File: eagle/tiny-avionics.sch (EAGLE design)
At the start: 67 parts, among them J1 USB-MICROB, J3 JST-PH-2-SMT-RA, U1 LP5907, U2 M25P10-AVMN6TP_TR, U3 LSM9DS0, U5 LTC1998, U6 ATMEGA32U4-AU, X1 8MHz

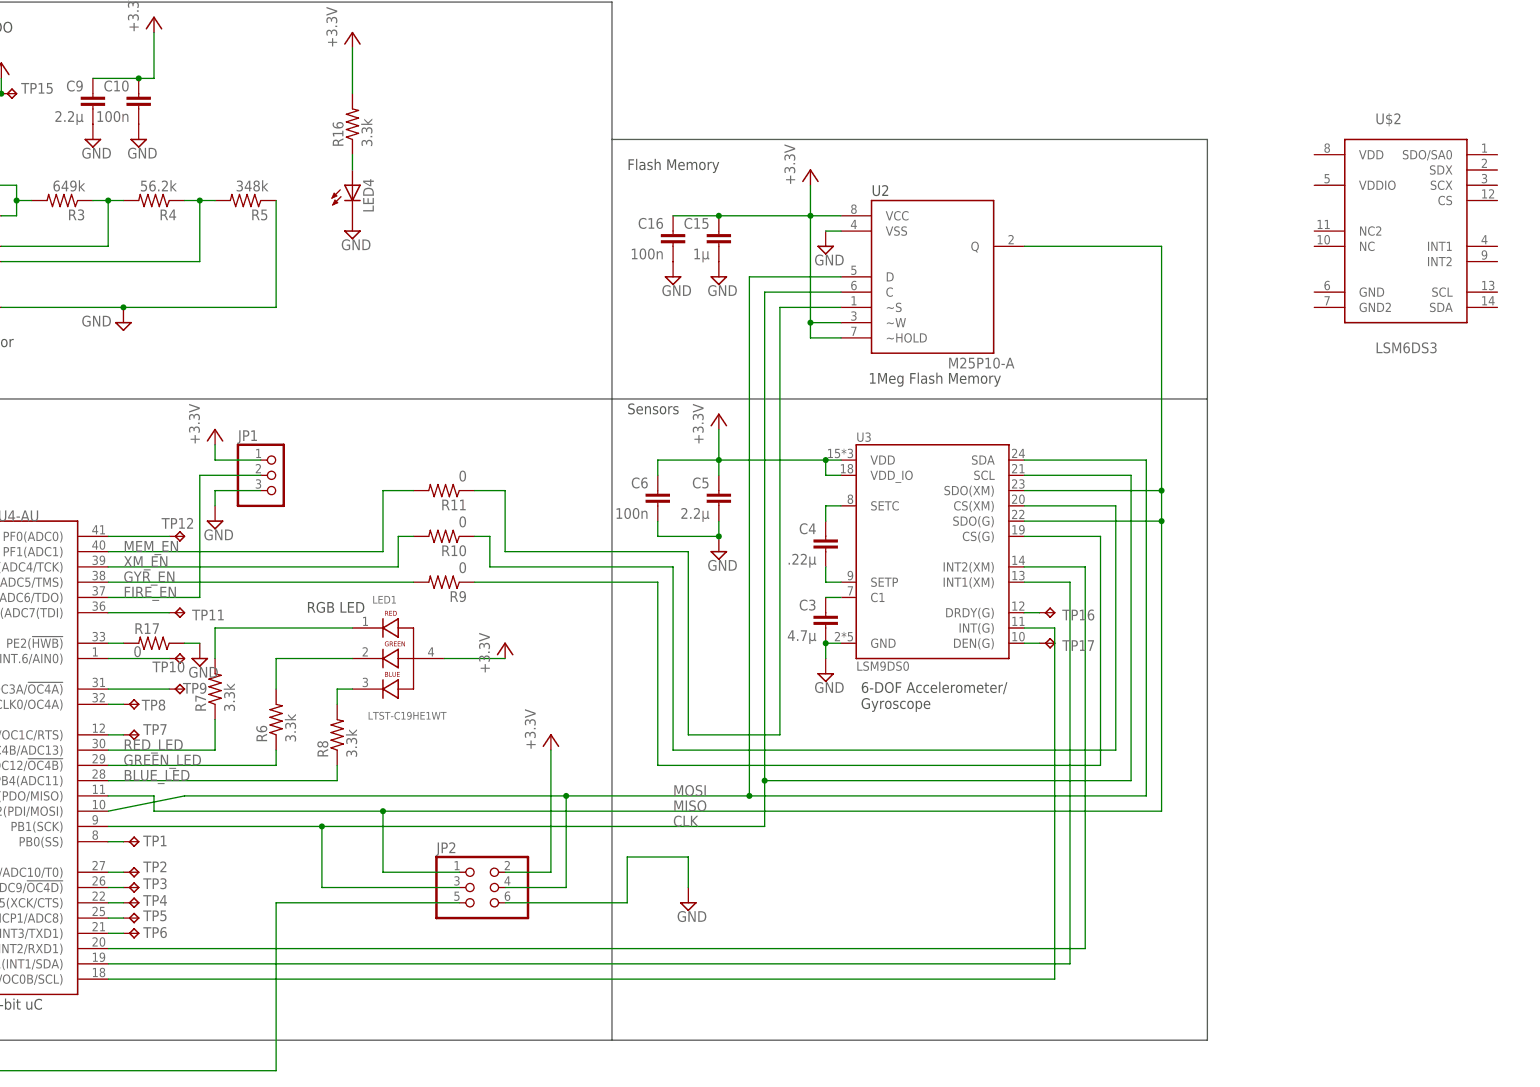
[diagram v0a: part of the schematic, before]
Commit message: Schematic work and created new device for 8-pin SPI memory chip.
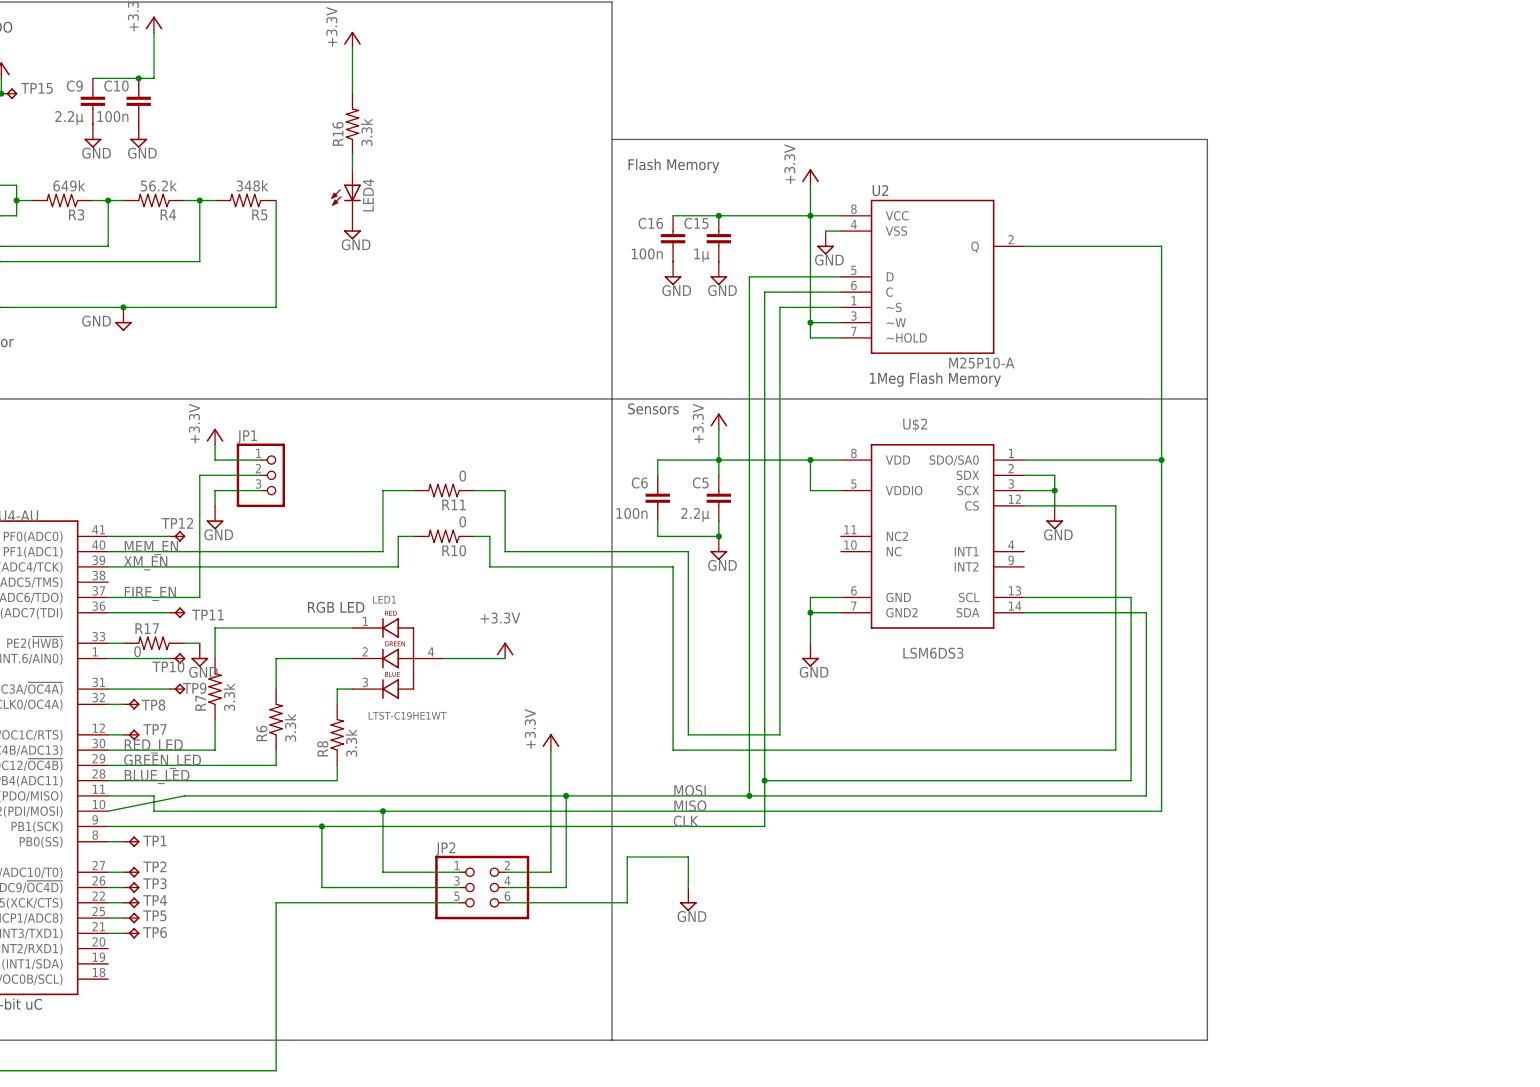
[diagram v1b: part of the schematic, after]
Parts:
- removed C3: 4.7µ, rcl:C-EUC0603
- removed C4: .22µ, rcl:C-EUC0603
- removed R9: 0, rcl:R-US_R0603
- removed TP16, TP17: TPTP08R, testpad:TPTP08R
- removed U3: LSM9DS0, LSM9DS0:LSM9DS0
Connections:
- removed net GYR_EN: R9.1, U3.CS(G)
- removed net N$10: C4.2, U3.SETC
- removed net N$11: C4.1, U3.SETP
- removed net N$16: U3.INT2(XM), U6.PD2(INT2/RXD1)
- removed net N$17: U3.INT1(XM), U6.PD1(INT1/SDA)
- removed net N$19: U3.INT(G), U6.PD0(INT0/OC0B/SCL)
- removed net N$20: R9.2, U6.PF5(ADC5/TMS)
- removed net N$66: TP17.TP, U3.DEN(G)
- removed net N$67: TP16.TP, U3.DRDY(G)
- removed net N$9: C3.2, U3.C1
- net CLK: now also U$2.SCL; no longer U3.SCL
- net GND: now also U$2.GND, U$2.GND2, U$2.SCX, U$2.SDX; no longer C3.1, U3.GND
- net MISO: now also U$2.SDO/SA0; no longer U3.SDO(G), U3.SDO(XM)
- net MOSI: now also U$2.SDA; no longer U3.SDA
- net VCC: now also U$2.VDD, U$2.VDDIO; no longer U3.VDD, U3.VDD_IO
- net XM_EN: now also U$2.CS; no longer U3.CS(XM)
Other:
- note removed: "6-DOF Accelerometer/ Gyroscope"
- moved on the sheet: U$2

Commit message: Working changes to schematic and layout.
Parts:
- removed U2: M25P10-AVMN6TP_TR, SOIC127P600X175-8N:M25P10-AVMN6TP_TR
- added U$3: M25PX16, tinyav-lib:M25PX16
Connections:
- new net N$10: U$2.INT1, U6.PD0(INT0/OC0B/SCL)
- new net N$11: U$2.INT2, U6.PD1(INT1/SDA)
- net CLK: now also U$3.CLK; no longer U2.C
- net GND: now also U$3.VSS; no longer U2.VSS
- net MEM_EN: now also U$3./S; no longer U2.~S
- net MISO: now also U$3.DQ1(MISO); no longer U2.Q
- net MOSI: now also U$3.DQ0(MOSI); no longer U2.D
- net VCC: now also U$3./HOLD, U$3./WP, U$3.VCC; no longer U2.VCC, U2.~HOLD, U2.~W
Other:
- note added: "16Meg Flash Memory"
- note removed: "1Meg Flash Memory"
- moved on the sheet: C15, C16, C5, C6, R6, R7, TP9

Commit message: Continued layout work.
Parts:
- R1, R15: device rcl:R-US_R0805 -> rcl:R-US_R0603
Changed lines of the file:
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@@
 <grid distance="0.1" unitdist="inch" unit="inch" style="lines" multiple="1" display="no" altdistance="0.01" altunitdist="inch" altunit="inch"/>
 <layers>
-<layer number="1" name="Top" color="4" fill="1" visible="no" active="no"/>
-<layer number="16" name="Bottom" color="1" fill="1" visible="no" active="no"/>
-<layer number="17" name="Pads" color="2" fill="1" visible="no" active="no"/>
-<layer number="18" name="Vias" color="2" fill="1" visible="no" active="no"/>
-<layer number="19" name="Unrouted" color="6" fill="1" visible="no" active="no"/>
-<layer number="20" name="Dimension" color="15" fill="1" visible="no" active="no"/>
-<layer number="21" name="tPlace" color="7" fill="1" visible="no" active="no"/>
-<layer number="22" name="bPlace" color="7" fill="1" visible="no" active="no"/>
-<layer number="23" name="tOrigins" color="15" fill="1" visible="no" active="no"/>
-<layer number="24" name="bOrigins" color="15" fill="1" visible="no" active="no"/>
-<layer number="25" name="tNames" color="7" fill="1" visible="no" active="no"/>
-<layer number="26" name="bNames" color="7" fill="1" visible="no" active="no"/>
-<layer number="27" name="tValues" color="7" fill="1" visible="no" active="no"/>
-<layer number="28" name="bValues" color="7" fill="1" visible="no" active="no"/>
+<layer number="1" name="Top" color="4" fill="1" visible="yes" active="no"/>
+<layer number="16" name="Bottom" color="1" fill="1" visible="yes" active="no"/>
+<layer number="17" name="Pads" color="2" fill="1" visible="yes" active="no"/>
+<layer number="18" name="Vias" color="2" fill="1" visible="yes" active="no"/>
+<layer number="19" name="Unrouted" color="6" fill="1" visible="yes" active="no"/>
+<layer number="20" name="Dimension" color="15" fill="1" visible="yes" active="no"/>
+<layer number="21" name="tPlace" color="7" fill="1" visible="yes" active="no"/>
+<layer number="22" name="bPlace" color="7" fill="1" visible="yes" active="no"/>
+<layer number="23" name="tOrigins" color="15" fill="1" visible="yes" active="no"/>
+<layer number="24" name="bOrigins" color="15" fill="1" visible="yes" active="no"/>
+<layer number="25" name="tNames" color="7" fill="1" visible="yes" active="no"/>
+<layer number="26" name="bNames" color="7" fill="1" visible="yes" active="no"/>
+<layer number="27" name="tValues" color="7" fill="1" visible="yes" active="no"/>
+<layer number="28" name="bValues" color="7" fill="1" visible="yes" active="no"/>
 <layer number="29" name="tStop" color="7" fill="3" visible="no" active="no"/>
 <layer number="30" name="bStop" color="7" fill="6" visible="no" active="no"/>
@@
 <layer number="35" name="tGlue" color="7" fill="4" visible="no" active="no"/>
 <layer number="36" name="bGlue" color="7" fill="5" visible="no" active="no"/>
-<layer number="37" name="tTest" color="7" fill="1" visible="no" active="no"/>
-<layer number="38" name="bTest" color="7" fill="1" visible="no" active="no"/>
+<layer number="37" name="tTest" color="7" fill="1" visible="yes" active="no"/>
+<layer number="38" name="bTest" color="7" fill="1" visible="yes" active="no"/>
 <layer number="39" name="tKeepout" color="4" fill="11" visible="no" active="no"/>
 <layer number="40" name="bKeepout" color="1" fill="11" visible="no" active="no"/>
@@
 <layer number="44" name="Drills" color="7" fill="1" visible="no" active="no"/>
 <layer number="45" name="Holes" color="7" fill="1" visible="no" active="no"/>
-<layer number="46" name="Milling" color="3" fill="1" visible="no" active="no"/>
-<layer number="47" name="Measures" color="7" fill="1" visible="no" active="no"/>
-<layer number="48" name="Document" color="7" fill="1" visible="no" active="no"/>
-<layer number="49" name="Reference" color="7" fill="1" visible="no" active="no"/>
-<layer number="50" name="dxf" color="7" fill="1" visible="no" active="no"/>
-<layer number="51" name="tDocu" color="7" fill="1" visible="no" active="no"/>
-<layer number="52" name="bDocu" color="7" fill="1" visible="no" active="no"/>
-<layer number="53" name="tGND_GNDA" color="7" fill="9" visible="no" active="no"/>
-<layer number="54" name="bGND_GNDA" color="1" fill="9" visible="no" active="no"/>
-<layer number="56" name="wert" color="7" fill="1" visible="no" active="no"/>
-<layer number="57" name="tCAD" color="7" fill="1" visible="no" active="no"/>
-<layer number="59" name="tCarbon" color="7" fill="1" visible="no" active="no"/>
-<layer number="60" name="bCarbon" color="7" fill="1" visible="no" active="no"/>
+<layer number="46" name="Milling" color="3" fill="1" visible="yes" active="no"/>
+<layer number="47" name="Measures" color="7" fill="1" visible="yes" active="no"/>
+<layer number="48" name="Document" color="7" fill="1" visible="yes" active="no"/>
+<layer number="49" name="Reference" color="7" fill="1" visible="yes" active="no"/>
+<layer number="50" name="dxf" color="7" fill="1" visible="yes" active="no"/>
+<layer number="51" name="tDocu" color="7" fill="1" visible="yes" active="no"/>
+<layer number="52" name="bDocu" color="7" fill="1" visible="yes" active="no"/>
+<layer number="53" name="tGND_GNDA" color="7" fill="9" visible="yes" active="no"/>
+<layer number="54" name="bGND_GNDA" color="1" fill="9" visible="yes" active="no"/>
+<layer number="56" name="wert" color="7" fill="1" visible="yes" active="no"/>
+<layer number="57" name="tCAD" color="7" fill="1" visible="yes" active="no"/>
+<layer number="59" name="tCarbon" color="7" fill="1" visible="yes" active="no"/>
+<layer number="60" name="bCarbon" color="7" fill="1" visible="yes" active="no"/>
 <layer number="90" name="Modules" color="5" fill="1" visible="yes" active="yes"/>
 <layer number="91" name="Nets" color="2" fill="1" visible="yes" active="yes"/>
@@
 <part name="R13" library="rcl" deviceset="R-US_" device="R0603" value="22"/>
 <part name="LED2" library="adafruit" deviceset="LED" device="CHIP-LED0603"/>
-<part name="R15" library="rcl" deviceset="R-US_" device="R0805" value="3.3k"/>
+<part name="R15" library="rcl" deviceset="R-US_" device="R0603" value="3.3k"/>
 <part name="JP2" library="pinhead" deviceset="PINHD-2X3" device=""/>
 <part name="SUPPLY8" library="supply2" deviceset="GND" device=""/>
@@
 <part name="U$1" library="tinyav-lib" deviceset="BQ21040" device=""/>
 <part name="SUPPLY1" library="supply2" deviceset="GND" device=""/>
-<part name="R1" library="rcl" deviceset="R-US_" device="R0805" value="5.36k"/>
+<part name="R1" library="rcl" deviceset="R-US_" device="R0603" value="5.36k"/>
 <part name="SUPPLY3" library="supply2" deviceset="GND" device=""/>
 <part name="U$2" library="tinyav-lib" deviceset="LSM6DS3" device=""/>

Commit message: More layout work.  Removed a bypass capacitor we didn't really need.
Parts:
- removed C9: 2.2µ, rcl:C-EUC0603
- C2: device rcl:C-EUC0805 -> rcl:C-EUC0603
- R16, R2, R6, R7, R8: device rcl:R-US_R0805 -> rcl:R-US_R0603
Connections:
- net N$52 renamed TP3
- net N$54 renamed TP12
- net N$55 renamed TP11
- net N$56 renamed TP10
- net N$57 renamed TP9
- net N$58 renamed TP8
- net N$59 renamed TP7
- net N$60 renamed TP1
- net N$61 renamed TP2
- net N$62 renamed TP4
- net N$63 renamed TP5
- net N$64 renamed TP6
- net GND: no longer C9.2
- net VCC: no longer C9.1
